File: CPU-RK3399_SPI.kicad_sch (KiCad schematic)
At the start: 1 part, among them U1 RK3399

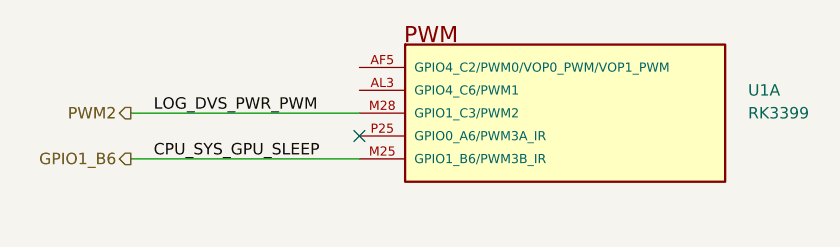
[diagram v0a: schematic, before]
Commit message: update schematic
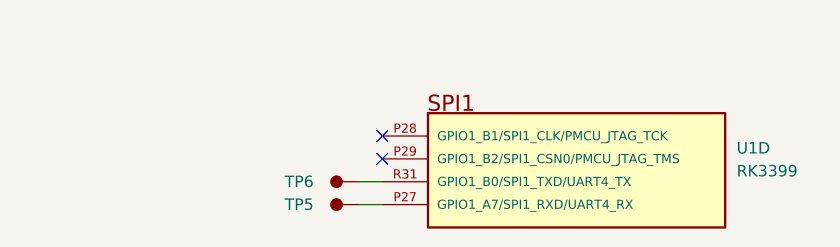
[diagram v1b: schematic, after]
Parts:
- removed U1: RK3399, footprints:BGA828C65P31X31_2100X2100X161, symbol component_library:System On Chip (SoC)/RK3399
- added TP5, TP6: ~, footprints:, symbol component_library:Mechanical/Test_Point
- added U1: RK3399, footprints:BGA828C65P31X31_2100X2100X161, symbol component_library:System On Chip (SoC)/RK3399
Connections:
- new net: TP5.TP, U1.P27 (GPIO1_A7/SPI1_RXD/UART4_RX)
- new net: TP6.TP, U1.R31 (GPIO1_B0/SPI1_TXD/UART4_TX)
- no-connect marks 1 -> 2
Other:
- title: (none) -> CPU-RK3399 SPI Controller
